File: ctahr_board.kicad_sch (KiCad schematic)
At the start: 0 parts

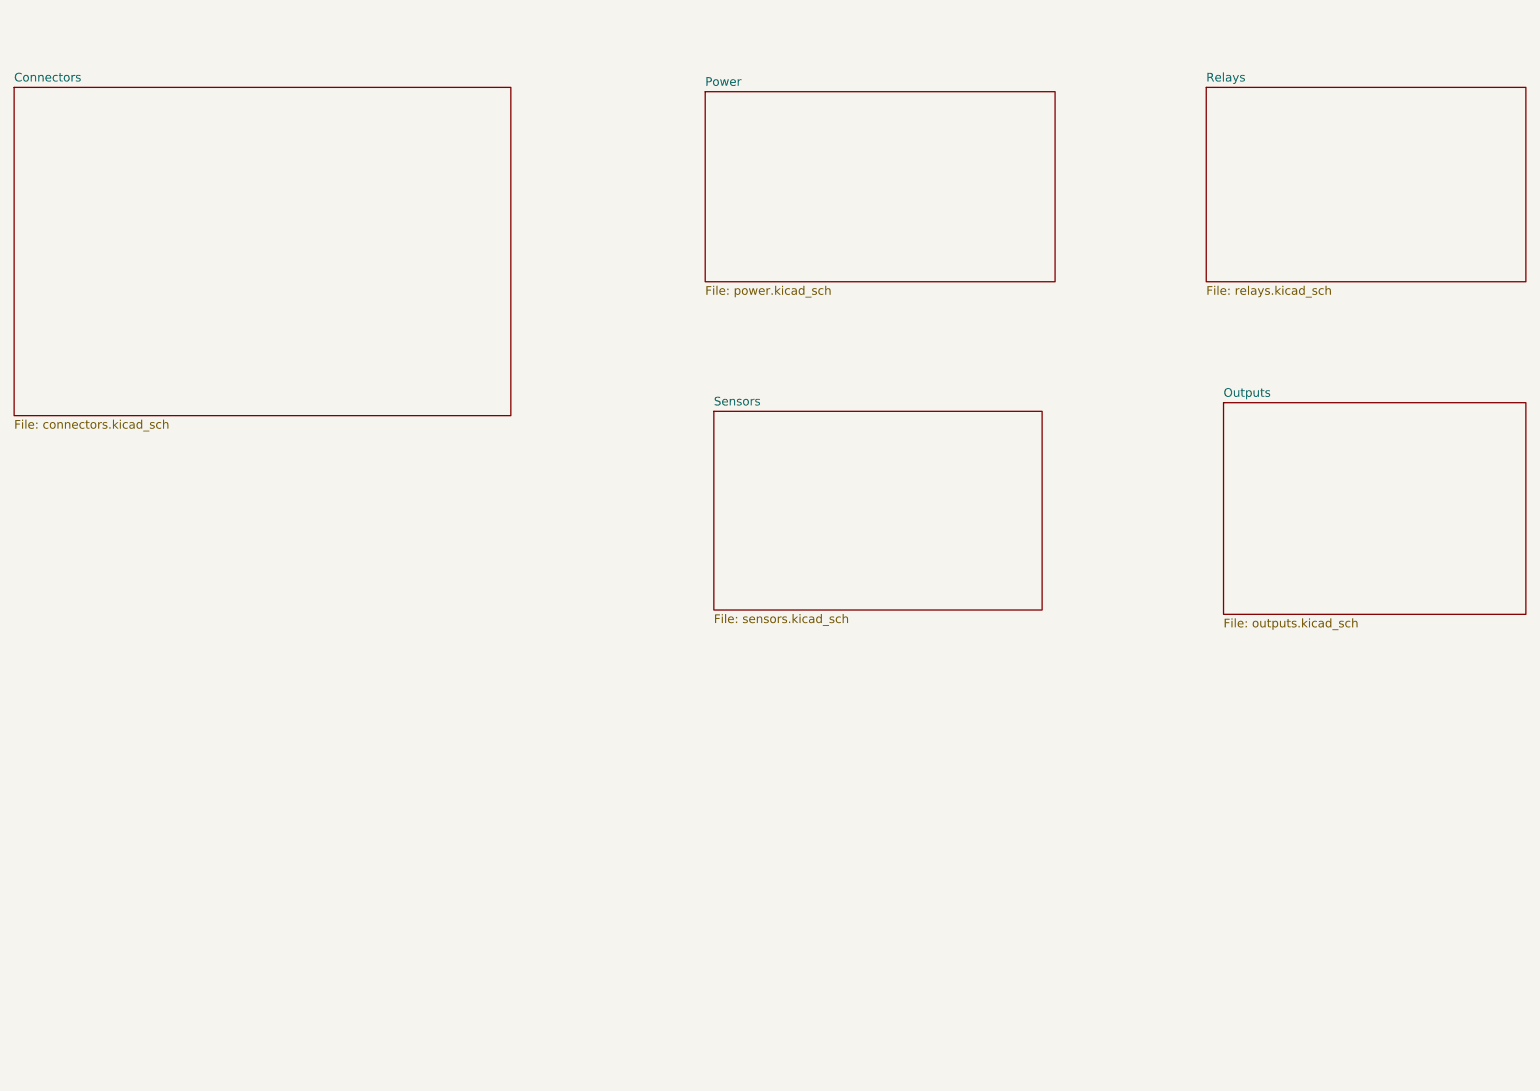
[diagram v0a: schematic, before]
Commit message: Added power surge protection
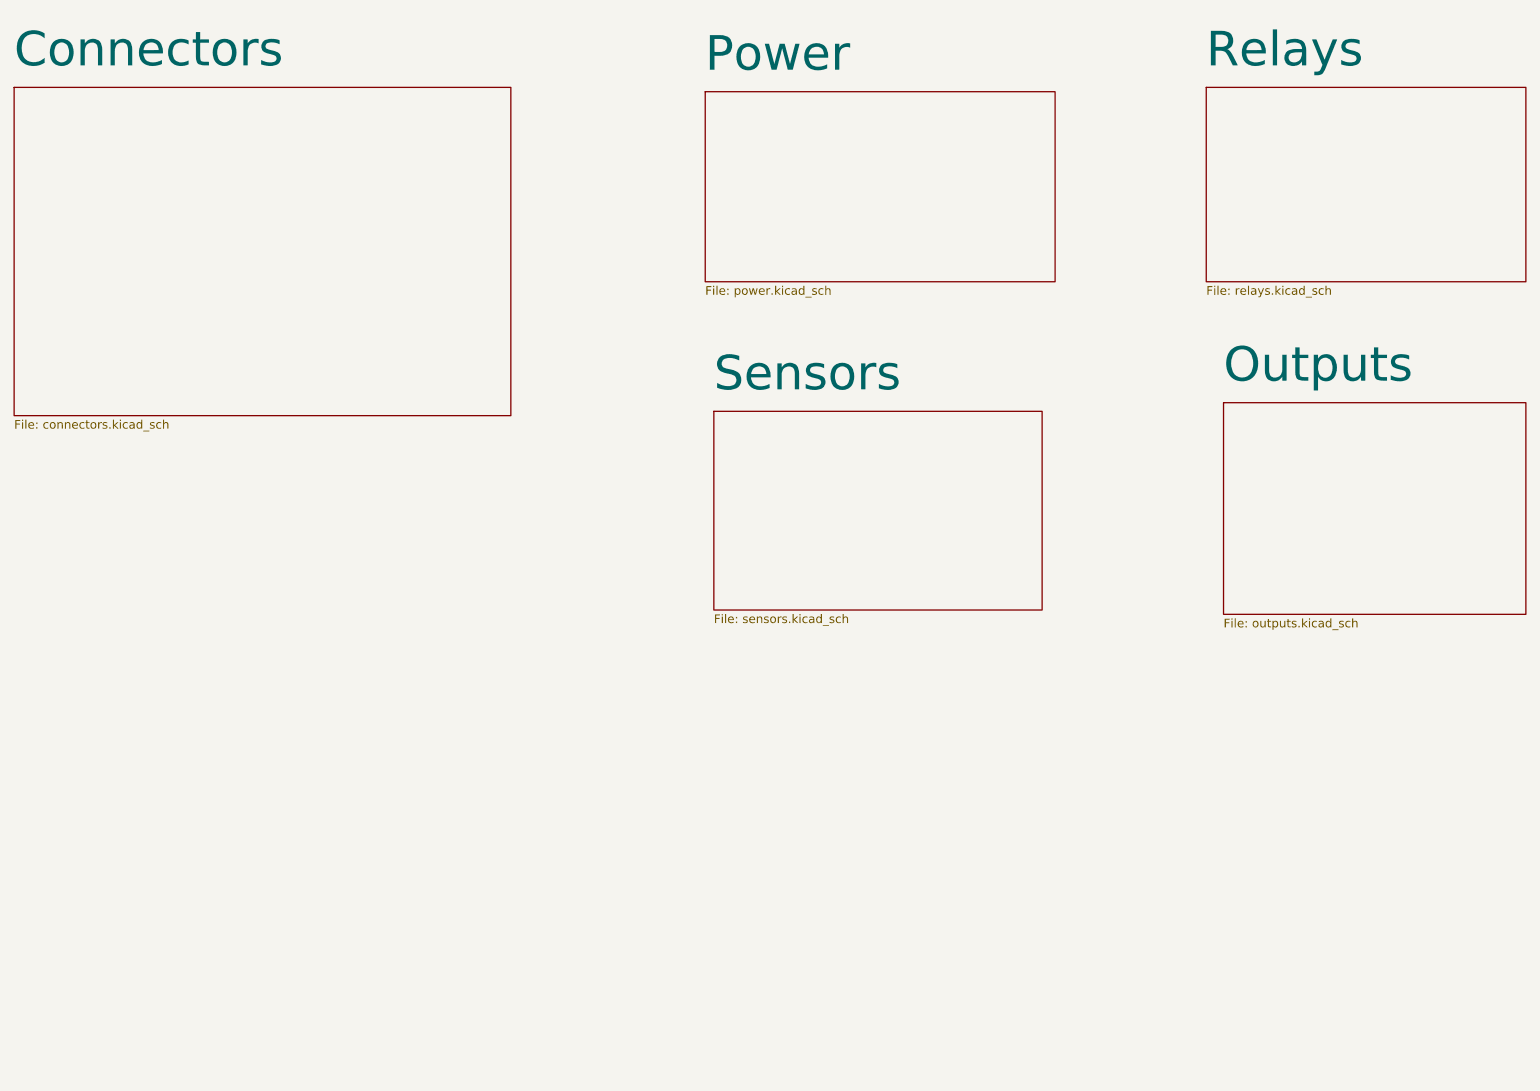
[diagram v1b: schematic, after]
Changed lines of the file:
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@@
 		)
 		(property "Sheetname" "Sensors"
-			(at 132.08 76.7584 0)
+			(at 132.08 74.8534 0)
 			(effects
 				(font
-					(size 1.27 1.27)
+					(size 5.08 5.08)
 				)
 				(justify left bottom)
@@
 		)
 		(property "Sheetname" "Power"
-			(at 130.81 29.7684 0)
+			(at 130.81 27.8634 0)
 			(effects
 				(font
-					(size 1.27 1.27)
+					(size 5.08 5.08)
 				)
 				(justify left bottom)
@@
 		)
 		(property "Sheetname" "Outputs"
-			(at 207.01 75.4884 0)
+			(at 207.01 73.5834 0)
 			(effects
 				(font
-					(size 1.27 1.27)
+					(size 5.08 5.08)
 				)
 				(justify left bottom)
@@
 		)
 		(property "Sheetname" "Connectors"
-			(at 29.21 29.1334 0)
+			(at 29.21 27.2284 0)
 			(effects
 				(font
-					(size 1.27 1.27)
+					(size 5.08 5.08)
 				)
 				(justify left bottom)
@@
 		)
 		(property "Sheetname" "Relays"
-			(at 204.47 29.1334 0)
+			(at 204.47 27.2284 0)
 			(effects
 				(font
-					(size 1.27 1.27)
+					(size 5.08 5.08)
 				)
 				(justify left bottom)

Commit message: All done, pending review
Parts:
- added U4: ~, Logos:taz, symbol Logos:Logo_TAZ
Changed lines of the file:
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@@
 	(generator_version "8.0")
 	(paper "A4")
+	(symbol
+		(lib_id "Logos:Logo_TAZ")
+		(at 40.64 176.53 0)
+		(unit 1)
+		(exclude_from_sim no)
+		(in_bom no)
+		(on_board yes)
+		(dnp no)
+		(fields_autoplaced yes)
+		(property "Reference" "U4"
+			(at 43.019 173.5208 0)
+			(effects
+				(font
+					(size 1.27 1.27)
+				)
+				(justify left)
+			)
+		)
+		(property "Value" "~"
+			(at 43.019 175.2022 0)
+			(effects
+				(font
+					(size 1.27 1.27)
+				)
+				(justify left)
+			)
+		)
+		(property "Footprint" "Logos:taz"
+			(at 40.64 176.53 0)
+			(effects
+				(font
+					(size 1.27 1.27)
+				)
+				(hide yes)
+			)
+		)
+		(property "Datasheet" ""
+			(at 40.64 176.53 0)
+			(effects
+				(font
+					(size 1.27 1.27)
+				)
+				(hide yes)
+			)
+		)
+		(property "Description" ""
+			(at 40.64 176.53 0)
+			(effects
+				(font
+					(size 1.27 1.27)
+				)
+				(hide yes)
+			)
+		)
+		(instances
+			(project ""
+				(path "/dea08218-351b-4b2b-ab50-f60349a3e49f"
+					(reference "U4")
+					(unit 1)
+				)
+			)
+		)
+	)
 	(sheet
 		(at 132.08 77.47)
